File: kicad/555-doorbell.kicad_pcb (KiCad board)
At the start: 2 copper layers, 44.7 x 41.7 mm, 14 parts, among them SW1 SW_PUSH_SMALL_H, U1 LM555N

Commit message: pcb v1 finished
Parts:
- added P1: CONN_01X02, Connect:PINHEAD1-2, F.Cu at (140.5, 87.1)
- SP1: footprint Connect:PINHEAD1-2 -> Buzzers_Beepers:BUZZER
- moved R2 9.89 mm to (151.5, 100.5), turned to 90 degrees
- moved R4 9.82 mm to (158.1, 90.3), turned to 270 degrees
- moved R1 9.01 mm to (128.3, 118.1), turned to 0 degrees
- moved C1 8.92 mm to (144.3, 93.7)
- moved C5 7.64 mm to (131.3, 103.1)
- moved D1 7.58 mm to (144.0, 110.0)
- moved C2 7.41 mm to (131.3, 109.0)
- moved U1 7.39 mm to (138.0, 97.5)
- moved D2 7.19 mm to (144.0, 113.5)
- moved R3 6.68 mm to (154.8, 90.3), turned to 270 degrees
- moved SW1 4.10 mm to (152.7, 115.3)
- moved C3 3.98 mm to (152.4, 106.9)
- moved C4 3.59 mm to (152.4, 110.2)
- moved SP1 2.96 mm to (129.5, 91.0)
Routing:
- net VCC: track 12.6 -> 67.3 mm
- net Net-(D1-Pad2): track 35.0 -> 19.9 mm
- net Net-(C3-Pad1): track 17.0 -> 26.6 mm
- net Net-(C4-Pad1): track 0.00 -> 9.56 mm
- net Net-(D2-Pad1): track 37.9 -> 46.9 mm
- net Net-(R3-Pad2): track 19.8 -> 22.9 mm
- net Net-(C2-Pad1): track 26.1 -> 27.2 mm
- net Net-(C5-Pad1): track 6.10 -> 6.91 mm
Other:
- board size 44.7 x 41.7 mm -> 45 x 45 mm
- board text added: "555-DoorBell"
- board text added: "by jaimelaborda"

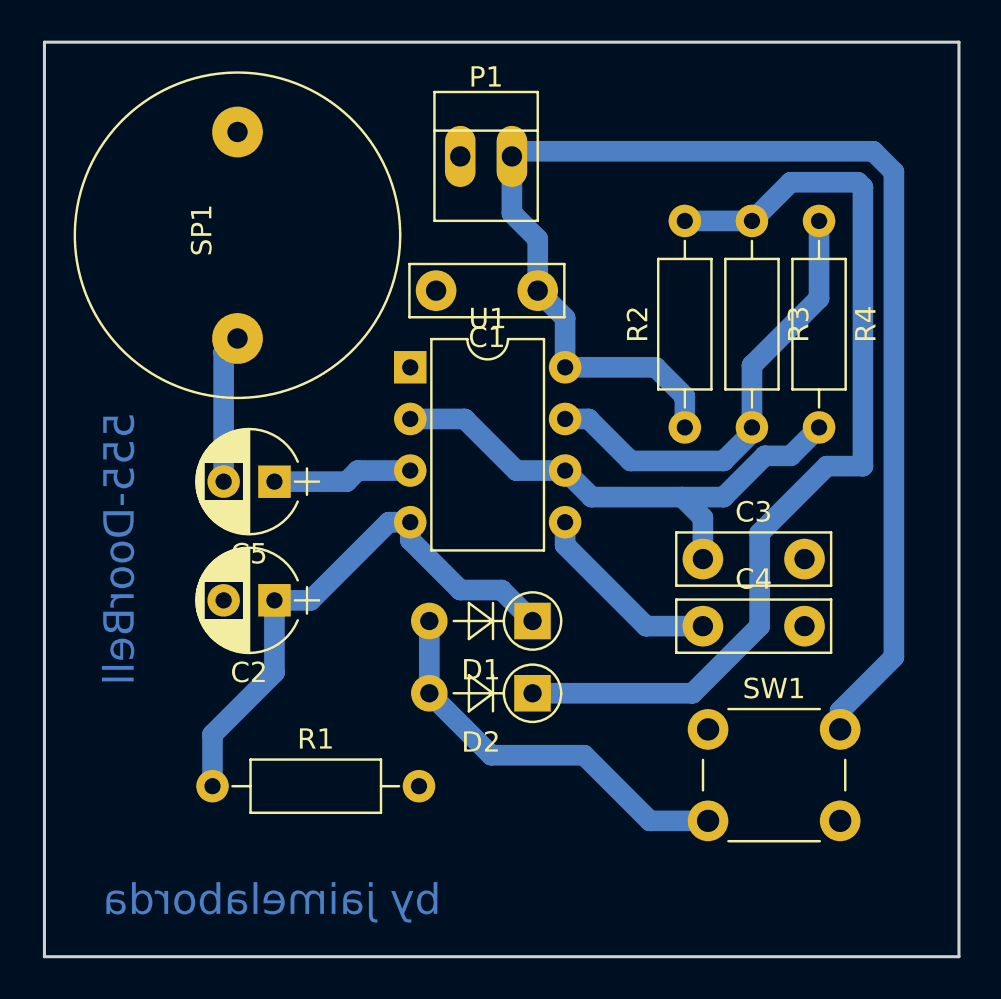
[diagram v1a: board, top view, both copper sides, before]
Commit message: Changes in the diammeter of the pads, re-do pdf
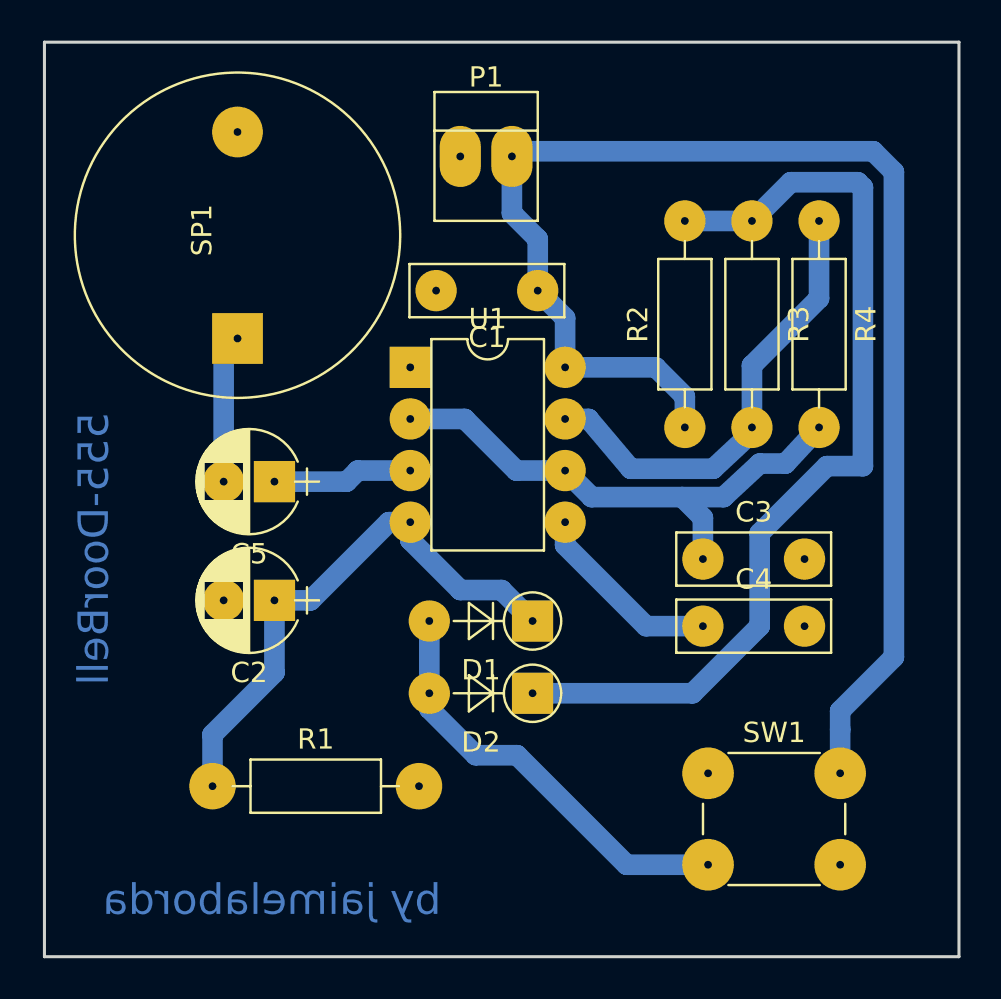
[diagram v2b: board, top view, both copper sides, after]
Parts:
- moved SW1 2.16 mm to (152.7, 117.5)
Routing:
- net VCC: track 67.3 -> 69.5 mm
- net Net-(D1-Pad2): track 19.9 -> 21.2 mm
